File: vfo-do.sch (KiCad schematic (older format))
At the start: 29 parts, among them P1 CONN_01X02, P2 Band, P3 Si5351, P4 Encoder, P5 GPS, P6 CONN_01X09, U1 LM317T, U2 MC78M05CDT, U3 MC78M05CDT, U4 Arduino_Nano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

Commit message: modif mineure sur un rappel de masse
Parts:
- RV1: symbol POT -> POT-RESCUE-vfo-do
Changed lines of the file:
@@
 EESchema Schematic File Version 2
+LIBS:vfo-do-rescue
 LIBS:power
 LIBS:device
@@
 $EndComp
 $Comp
-L POT RV1
+L POT-RESCUE-vfo-do RV1
 U 1 1 57138BF4
 P 9400 3950

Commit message: suppression des sorties filtres
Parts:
- removed C8: 100n, Capacitors_SMD:C_1206_HandSoldering, symbol C
- removed P6: CONN_01X09, Connectors_Molex:Molex_KK_6410-09, symbol CONN_01X09
- removed U5: ULN2803A, Housings_SOIC:SOIC-18_7.5x11.6mm_Pitch1.27mm, symbol ULN2803A
- removed U6: 4028, Housings_SOIC:SOIC-16_3.9x9.9mm_Pitch1.27mm, symbol 4028
- added P6: UP, Connectors_Molex:Molex_KK_6410-02, symbol CONN_01X02
- added P7: Band, Connectors_Molex:Molex_KK_6410-02, symbol CONN_01X02
- added P8: Reset, Connectors_Molex:Molex_KK-6410-02_02x2.54mm_Straight, symbol CONN_01X02
- P2: value Band -> DWN
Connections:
- net GND: now also P6.2 (P2), P7.2 (P2), P8.2 (P2)
- net at U4.10 (A6): no longer P3.7 (P7)
- net at U4.18 (Reset): now also P8.1 (P1)
- net at U4.23 (#D5): now also P3.7 (P7)
- net at U4.4 (A0): now also P2.1 (P1)
- net at U4.5 (A1): now also P6.1 (P1)
- net at U4.7 (A3): now also P7.1 (P1); no longer P2.1 (P1)
- no-connect marks 17 -> 14
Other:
- note removed: "+12 V\n\n"
- note removed: "Vers filtres \n2, 4, 8, 16\n32,64,128 MHz"

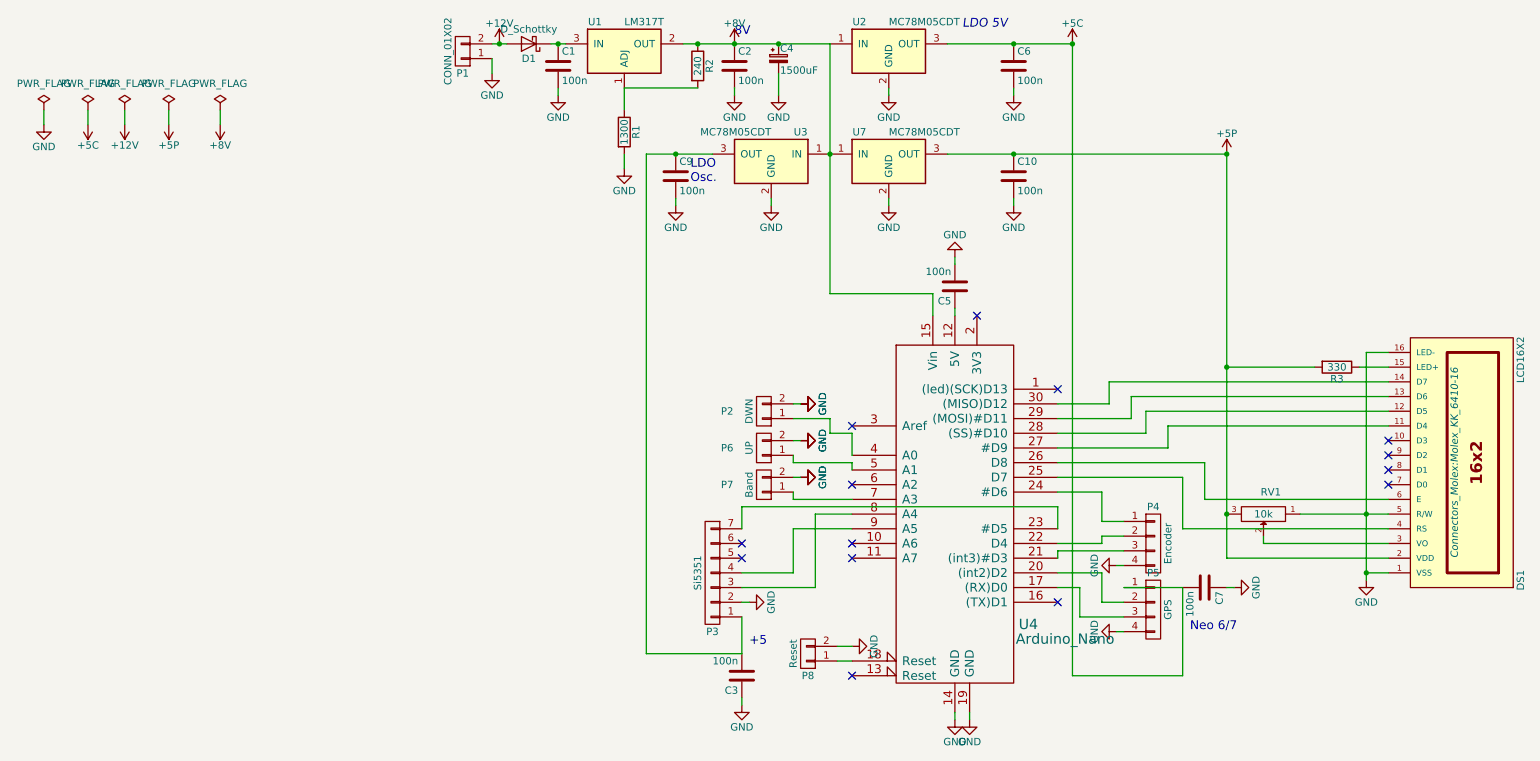
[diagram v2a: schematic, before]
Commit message: nettoyage routage, LM317 et Si5351 non verifie
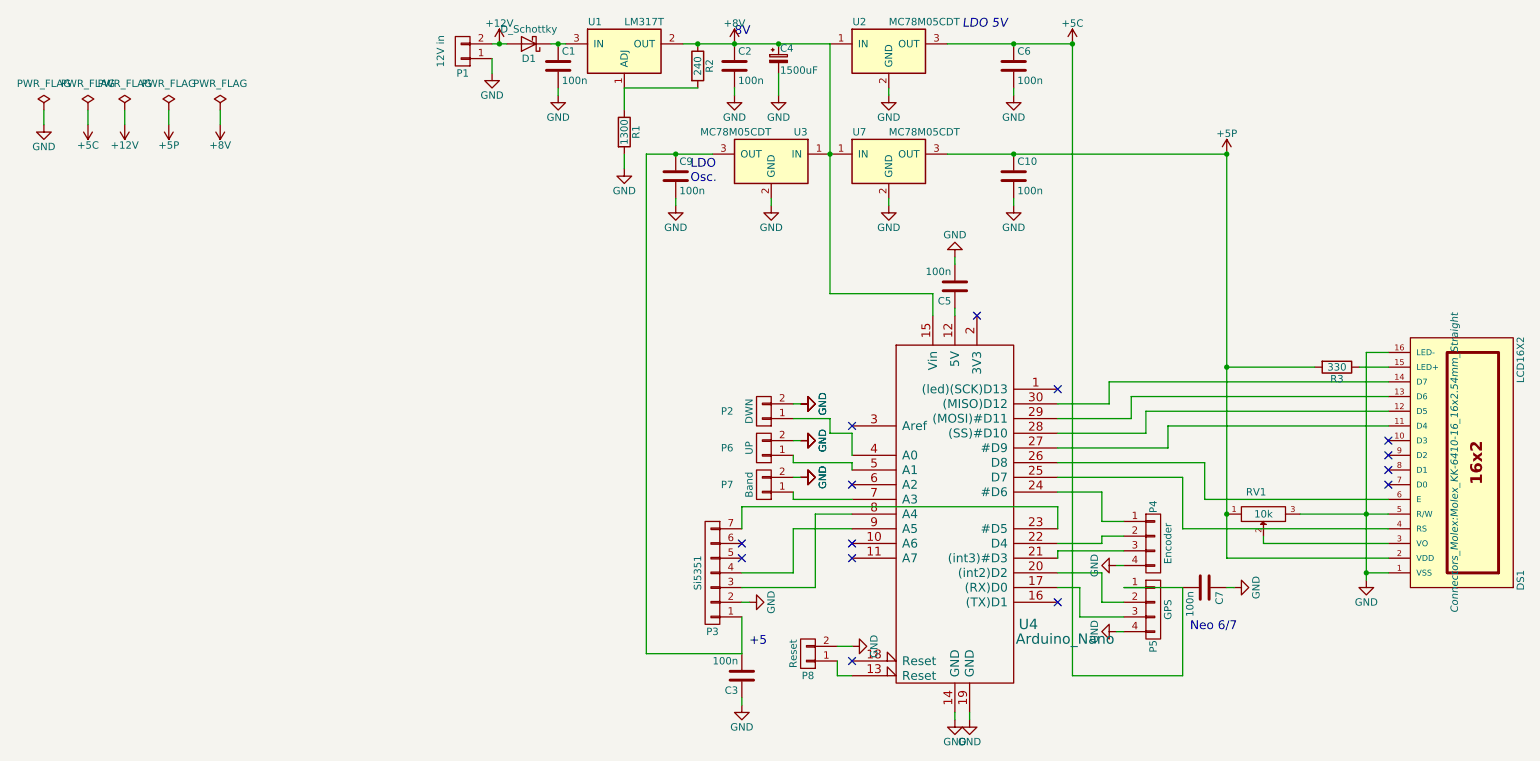
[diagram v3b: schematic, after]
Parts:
- DS1: footprint Connectors_Molex:Molex_KK_6410-16 -> Connectors_Molex:Molex_KK-6410-16_16x2.54mm_Straight
- P1: value CONN_01X02 -> 12V in; footprint Connectors_Molex:Molex_KK_6410-02 -> Connectors_Molex:Molex_KK-6410-02_02x2.54mm_Straight
- P2, P6, P7: footprint Connectors_Molex:Molex_KK_6410-02 -> Connectors_Molex:Molex_KK-6410-02_02x2.54mm_Straight
- P3: footprint Connectors_Molex:Molex_KK_6410-07 -> Connectors_Molex:Molex_KK-6410-07_07x2.54mm_Straight
- P4, P5: footprint Connectors_Molex:Molex_KK_6410-04 -> Connectors_Molex:Molex_KK-6410-04_04x2.54mm_Straight
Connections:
- net +5P: now also RV1.1; no longer RV1.3
- net GND: now also RV1.3; no longer RV1.1
- net at U4.13 (Reset): now also P8.1 (P1)
- net at U4.18 (Reset): no longer P8.1 (P1)
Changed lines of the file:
@@
 F 3 "" H 9400 3950 50  0000 C CNN
 	1    9400 3950
-	-1   0    0    1
+	1    0    0    1
 $EndComp
 $Comp
@@
 F 0 "DS1" H 9950 4000 50  0000 C CNN
 F 1 "LCD16X2" H 11450 4000 50  0000 C CNN
-F 2 "Connectors_Molex:Molex_KK_6410-16" H 10750 3550 50  0000 C CIN
+F 2 "Connectors_Molex:Molex_KK-6410-16_16x2.54mm_Straight" H 10750 3550 50  0000 C CIN
 F 3 "" H 10750 3600 50  0000 C CNN
 	1    10750 3600
@@
 U 1 1 57139983
 P 8650 4600
-F 0 "P5" H 8650 4850 50  0000 C CNN
+F 0 "P5" V 8650 4350 50  0000 C CNN
 F 1 "GPS" V 8750 4600 50  0000 C CNN
-F 2 "Connectors_Molex:Molex_KK_6410-04" H 8650 4600 50  0001 C CNN
+F 2 "Connectors_Molex:Molex_KK-6410-04_04x2.54mm_Straight" H 8650 4600 50  0001 C CNN
 F 3 "" H 8650 4600 50  0000 C CNN
 	1    8650 4600
@@
 F 0 "P3" H 5650 4750 50  0000 C CNN
 F 1 "Si5351" V 5750 4350 50  0000 C CNN
-F 2 "Connectors_Molex:Molex_KK_6410-07" H 5650 4350 50  0001 C CNN
+F 2 "Connectors_Molex:Molex_KK-6410-07_07x2.54mm_Straight" H 5650 4350 50  0001 C CNN
 F 3 "" H 5650 4350 50  0000 C CNN
 	1    5650 4350
@@
 U 1 1 57139B2F
 P 8650 4150
-F 0 "P4" H 8650 4400 50  0000 C CNN
+F 0 "P4" V 8650 4400 50  0000 C CNN
 F 1 "Encoder" V 8750 4150 50  0000 C CNN
-F 2 "Connectors_Molex:Molex_KK_6410-04" H 8650 4150 50  0001 C CNN
+F 2 "Connectors_Molex:Molex_KK-6410-04_04x2.54mm_Straight" H 8650 4150 50  0001 C CNN
 F 3 "" H 8650 4150 50  0000 C CNN
 	1    8650 4150
@@
 P 3950 800
 F 0 "P1" H 3950 950 50  0000 C CNN
-F 1 "CONN_01X02" V 4050 800 50  0000 C CNN
-F 2 "Connectors_Molex:Molex_KK_6410-02" H 3950 800 50  0001 C CNN
+F 1 "12V in" V 4100 800 50  0000 C CNN
+F 2 "Connectors_Molex:Molex_KK-6410-02_02x2.54mm_Straight" H 3950 800 50  0001 C CNN
 F 3 "" H 3950 800 50  0000 C CNN
 	1    3950 800
@@
 Connection ~ 9150 2950
 Connection ~ 9150 3950
-NoConn ~ 6600 5050
+NoConn ~ 6600 4950
 NoConn ~ 6600 4250
 NoConn ~ 7450 2600
@@
 F 0 "P7" H 6250 3750 50  0000 C CNN
 F 1 "Band" V 6100 3750 50  0000 C CNN
-F 2 "Connectors_Molex:Molex_KK_6410-02" H 6000 3750 50  0001 C CNN
+F 2 "Connectors_Molex:Molex_KK-6410-02_02x2.54mm_Straight" H 6000 3750 50  0001 C CNN
 F 3 "" H 6000 3750 50  0000 C CNN
 	1    6000 3750
@@
 $EndComp
 Wire Wire Line
-	6600 4950 6500 4950
-Wire Wire Line
 	6600 4850 6500 4850
 $Comp
@@
 F 0 "P6" H 6250 3500 50  0000 C CNN
 F 1 "UP" V 6100 3500 50  0000 C CNN
-F 2 "Connectors_Molex:Molex_KK_6410-02" H 6000 3500 50  0001 C CNN
+F 2 "Connectors_Molex:Molex_KK-6410-02_02x2.54mm_Straight" H 6000 3500 50  0001 C CNN
 F 3 "" H 6000 3500 50  0000 C CNN
 	1    6000 3500
@@
 F 0 "P2" H 6250 3250 50  0000 C CNN
 F 1 "DWN" V 6100 3250 50  0000 C CNN
-F 2 "Connectors_Molex:Molex_KK_6410-02" H 6000 3250 50  0001 C CNN
+F 2 "Connectors_Molex:Molex_KK-6410-02_02x2.54mm_Straight" H 6000 3250 50  0001 C CNN
 F 3 "" H 6000 3250 50  0000 C CNN
 	1    6000 3250
@@
 NoConn ~ 6600 3750
 NoConn ~ 6600 4150
+Wire Wire Line
+	6500 4950 6500 5050
+Wire Wire Line
+	6500 5050 6600 5050
 $EndSCHEMATC
